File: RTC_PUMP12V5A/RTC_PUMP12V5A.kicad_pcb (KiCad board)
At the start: 2 copper layers, 80 x 80 mm, 66 parts, among them J1 12VDC_IN, J2 USB_C_Receptacle_USB2.0_16P, J3 Pump, J4 OLED SPI, J5 UART, J6 Conn_01x06_Socket, Q1 AO4407A, Q2 IRLR7843, SW1 SW_Push, SW2 SW_Push, U1 LM1117MP-3.3, U2 TPS5430DDA, U3 ESP32-C3-WROOM-02, U4 USBLC6-2SC6, U5 DS3231M

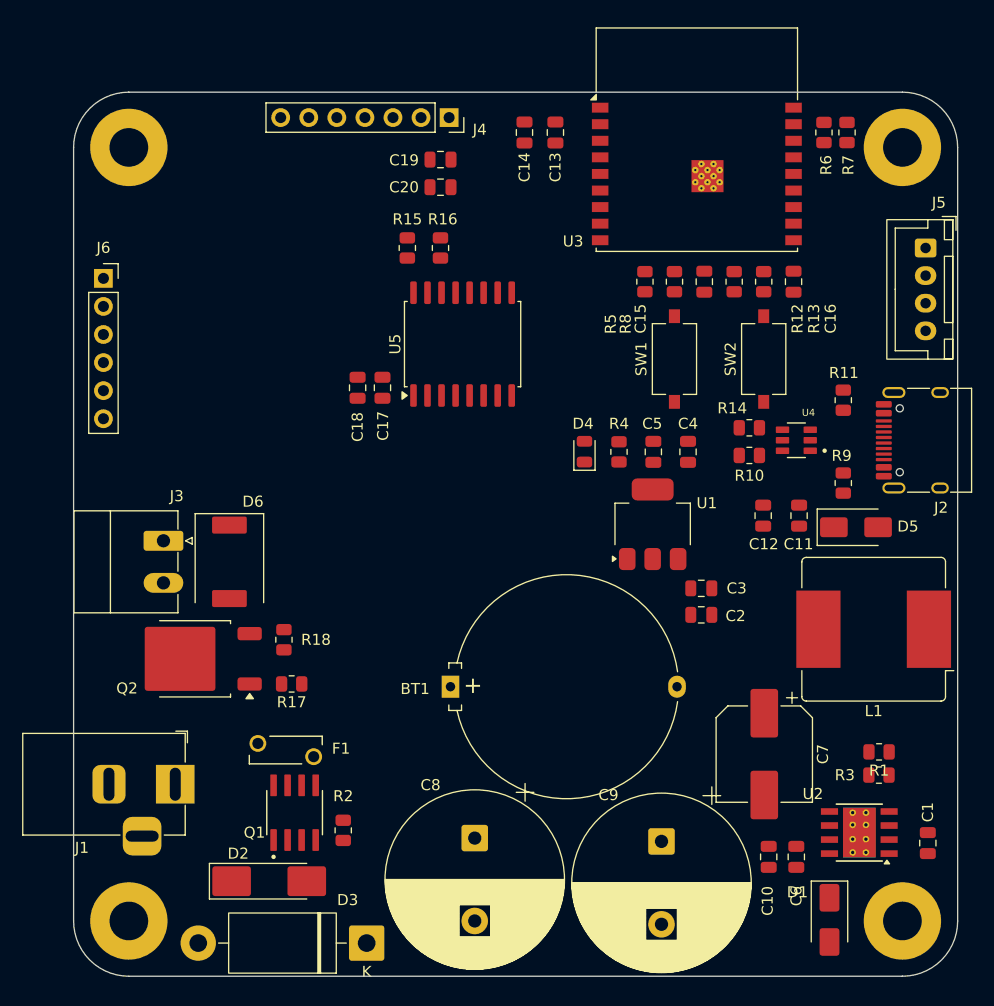
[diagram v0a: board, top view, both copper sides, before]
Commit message: layout completed RTC PUMP12V & push HBrigde project
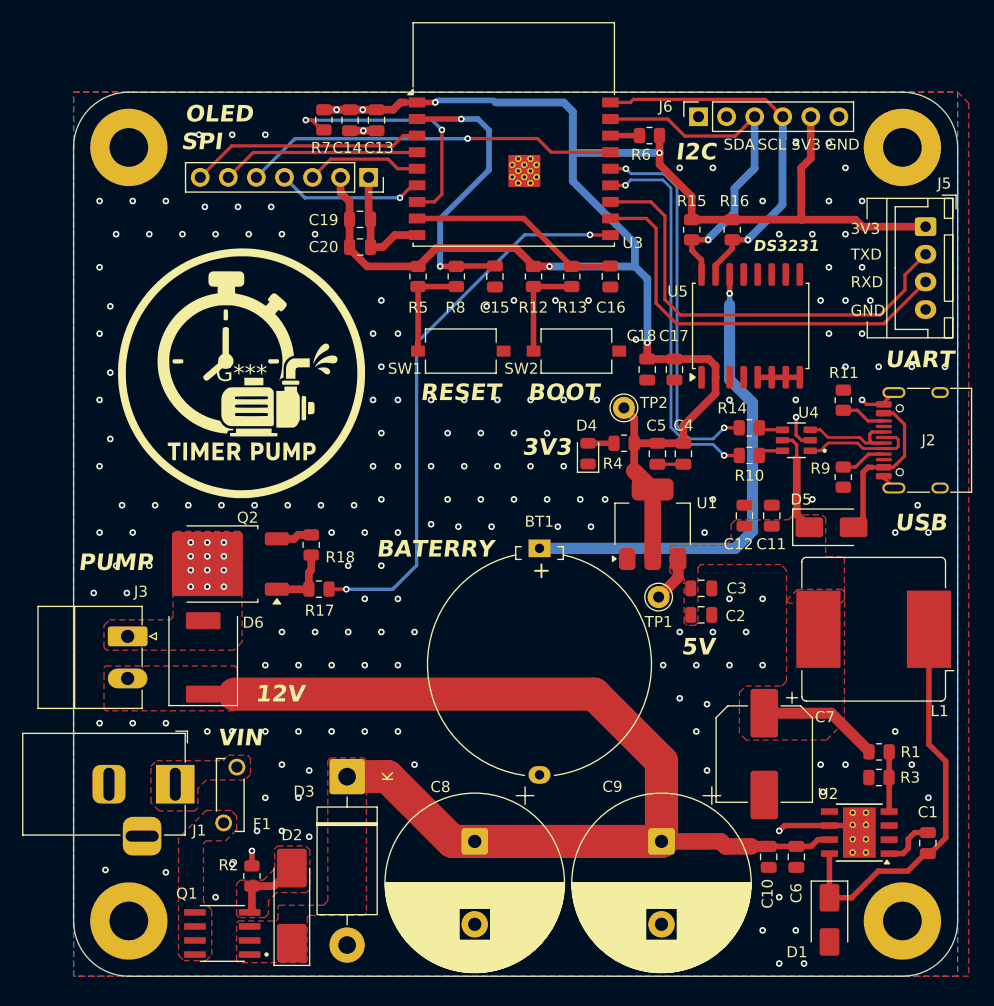
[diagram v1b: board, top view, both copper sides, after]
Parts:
- added G***: LOGO, PumpTimer:Logo, F.Cu at (126.7, 78.6)
- added TP1: TestPoint, Connector_Pin:Pin_D1.0mm_L10.0mm, F.Cu at (164.5, 98.8)
- added TP2: TestPoint, Connector_Pin:Pin_D1.0mm_L10.0mm, F.Cu at (161.3, 81.7)
- moved J6 55.8 mm to (168.1, 55.4), turned to 90 degrees
- moved R7 47.4 mm to (134.2, 55.7)
- moved C17 26.5 mm to (165.9, 78.3)
- moved R16 26.5 mm to (171.1, 65.6)
- moved C18 26.3 mm to (163.4, 78.3)
- moved U5 26.1 mm to (172.8, 74.3)
- moved R15 25.8 mm to (167.5, 65.6)
- moved R5 20.5 mm to (142.7, 69.8)
- moved R8 19.7 mm to (146.2, 69.8)
- moved SW1 19.3 mm to (146.6, 76.6), turned to 180 degrees
- moved C15 19.0 mm to (149.7, 69.8)
- moved R12 18.2 mm to (153.1, 69.8)
- moved R13 17.4 mm to (156.6, 69.8)
- moved SW2 17.0 mm to (157.0, 76.6), turned to 180 degrees
- moved C16 16.6 mm to (160.1, 69.8)
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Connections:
- J1 pad 3: (no net) -> GND
- J3 pad 1: VIN -> Net-(D6-A)
- J3 pad 2: Net-(D6-A) -> VIN
- J4 pad 6: IO10 -> IO5
- J4 pad 7: IO2 -> IO4
- J6 pad 3: IO9 -> IO1
- J6 pad 4: IO8 -> IO0
- R15 pad 1: IO9 -> IO1
- R16 pad 1: IO8 -> IO0
- U2 pad 5: EN -> EN_PWR
- U3 pad 10: IO10 -> PUMP
- U3 pad 3: PUMP -> IO4
- U5 pad 15: IO8 -> IO0
- U5 pad 16: IO9 -> IO1
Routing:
- net +3.3V: track 0.00 -> 164.8 mm, vias 0 -> 6
- net VIN: track 0.00 -> 97.7 mm
- net PUMP: track 0.00 -> 50.6 mm, vias 0 -> 2
- net Net-(U5-VBAT): track 0.00 -> 44.0 mm, vias 0 -> 1
- net IO21: track 0.00 -> 40.3 mm
- net GND: track 0.00 -> 39.2 mm, vias 0 -> 176
- net IO20: track 0.00 -> 38.0 mm
- net Net-(D1-K): track 0.00 -> 36.3 mm
- net USB_D+: track 0.00 -> 35.0 mm, vias 0 -> 2
- net USB_D-: track 0.00 -> 34.9 mm, vias 0 -> 2
- net IO3: track 0.00 -> 34.0 mm, vias 0 -> 1
- net IO0: track 0.00 -> 34.0 mm, vias 0 -> 1
- net IO1: track 0.00 -> 32.3 mm, vias 0 -> 1
- net EN: track 0.00 -> 26.1 mm, vias 0 -> 2
- net 5V: track 0.00 -> 24.5 mm
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- added copper zone on F.Cu, net 5V
- added copper zone on B.Cu, net GND
- added copper zone on F.Cu, net GND
- added copper zone on F.Cu, net Net-(D2-A)
- added copper zone on F.Cu, net Net-(D6-A)
- added copper zone on F.Cu, net Net-(F1-Pad1)
- added copper zone on F.Cu, net Net-(F1-Pad2)
- added copper zone on F.Cu, net VIN
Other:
- board text added: "12V"
- board text added: "3V3"
- board text added: "5V"
- board text added: "BATERRY"
- board text added: "BOOT"
- board text added: "DS3231"
- board text added: "GND"
- board text added: "I2C"
- board text added: "OLED"
- board text added: "PUMP"
- board text added: "RESET"
- board text added: "RXD"
- board text added: "SCL"
- board text added: "SDA"
- board text added: "SPI"
- board text added: "TXD"
- board text added: "UART"
- board text added: "USB"
- board text added: "VIN"
